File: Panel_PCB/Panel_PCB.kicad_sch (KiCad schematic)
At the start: 125 parts, among them J1 AC, J10 Relay 3, J11 Relay 4, J12 AC, J13 AC, J14 + de la bateria, J15 - de la bateria, J2 Bateria, J3 Sensor IN, J4 Sensor OUT, J5 Boton 1, J6 Boton 2, J7 Boton 3, J8 Relay 1, J9 Relay 2, K1 SANYOU_SRD_Form_C, K2 SANYOU_SRD_Form_C, K3 SANYOU_SRD_Form_C, K4 SANYOU_SRD_Form_C, K5 EC2-4.5SNU, K6 SANYOU_SRD_Form_C, K7 SANYOU_SRD_Form_C, Q1 2N2222A, Q2 2N2222A, Q3 2N2222A, Q4 2N2222A, Q5 BC558, Q6 BC558, Q7 2N2222A, U1 TLP291, U10 LM1117T-3.3, U11 LM7812_TO220, U2 TLP291, U3 TLP291, U4 TLP291, U5 LM7812_TO220, U6 LM7812_TO220, U7 LM7805_TO220, U8 LM7805_TO220, U9 LM1117T-3.3

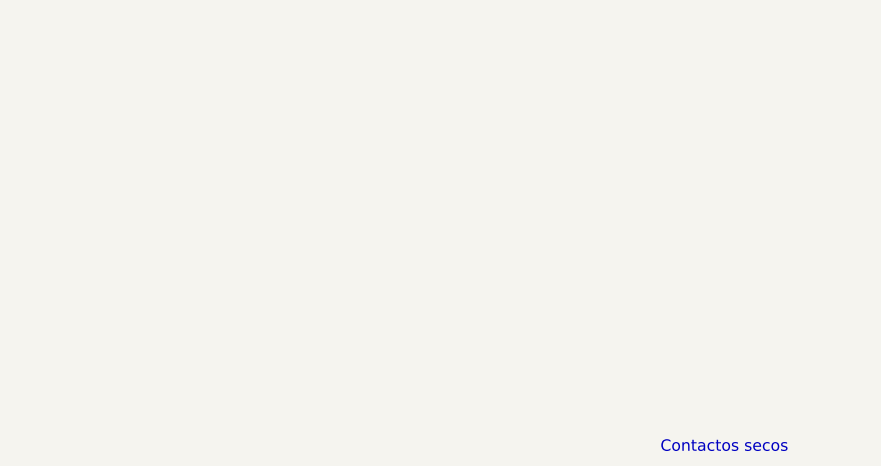
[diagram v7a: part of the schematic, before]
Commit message: DS1307 y bateria para mantener la hora actualizada
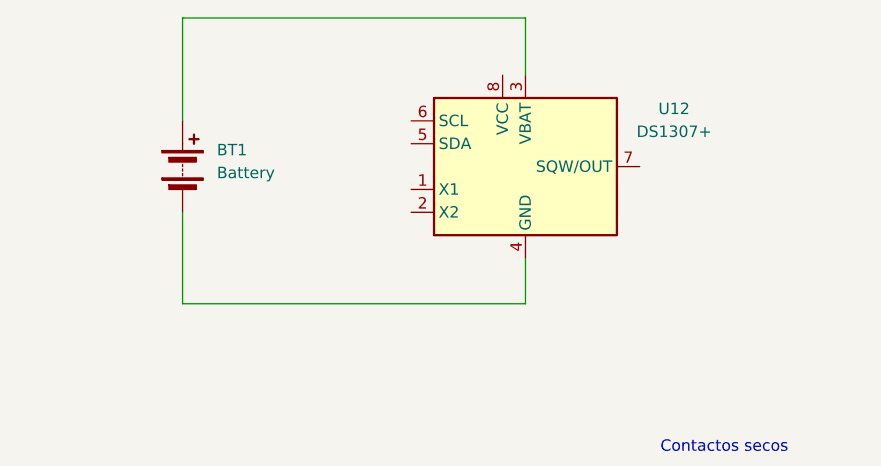
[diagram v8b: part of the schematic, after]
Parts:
- added BT1: Battery, Battery:BatteryHolder_Keystone_1060_1x2032, symbol Device:Battery
- added U12: DS1307+, Package_DIP:DIP-8_W7.62mm, symbol Timer_RTC:DS1307+
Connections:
- new net: BT1.1 (+), U12.3 (VBAT)
- new net: BT1.2 (-), U12.4 (GND)
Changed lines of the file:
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@@
 	(wire
 		(pts
+			(xy 445.77 72.39) (xy 445.77 67.31)
+		)
+		(stroke
+			(width 0)
+			(type default)
+			(color 0 0 0 1)
+		)
+	)
+	(wire
+		(pts
 			(xy 534.67 283.21) (xy 621.03 283.21)
 		)
@@
 	(wire
 		(pts
+			(xy 407.67 40.64) (xy 445.77 40.64)
+		)
+		(stroke
+			(width 0)
+			(type default)
+			(color 255 0 0 1)
+		)
+	)
+	(wire
+		(pts
 			(xy 154.94 110.49) (xy 154.94 120.65)
 		)
@@
 	(wire
 		(pts
+			(xy 445.77 40.64) (xy 445.77 46.99)
+		)
+		(stroke
+			(width 0)
+			(type default)
+			(color 255 0 0 1)
+		)
+	)
+	(wire
+		(pts
 			(xy 549.91 381) (xy 549.91 398.78)
 		)
@@
 	(wire
 		(pts
+			(xy 407.67 62.23) (xy 407.67 72.39)
+		)
+		(stroke
+			(width 0)
+			(type default)
+			(color 0 0 0 1)
+		)
+	)
+	(wire
+		(pts
 			(xy 273.05 233.68) (xy 273.05 247.65)
 		)
@@
 	(wire
 		(pts
+			(xy 407.67 52.07) (xy 407.67 40.64)
+		)
+		(stroke
+			(width 0)
+			(type default)
+			(color 255 0 0 1)
+		)
+	)
+	(wire
+		(pts
 			(xy 403.86 466.09) (xy 415.29 466.09)
 		)
@@
 	(wire
 		(pts
+			(xy 407.67 72.39) (xy 445.77 72.39)
+		)
+		(stroke
+			(width 0)
+			(type default)
+			(color 0 0 0 1)
+		)
+	)
+	(wire
+		(pts
 			(xy 403.86 300.99) (xy 403.86 339.09)
 		)
@@
 	)
 	(symbol
+		(lib_id "Device:Battery")
+		(at 407.67 57.15 0)
+		(unit 1)
+		(exclude_from_sim no)
+		(in_bom yes)
+		(on_board yes)
+		(dnp no)
+		(fields_autoplaced yes)
+		(property "Reference" "BT1"
+			(at 411.48 55.3084 0)
+			(effects
+				(font
+					(size 1.27 1.27)
+				)
+				(justify left)
+			)
+		)
+		(property "Value" "Battery"
+			(at 411.48 57.8484 0)
+			(effects
+				(font
+					(size 1.27 1.27)
+				)
+				(justify left)
+			)
+		)
+		(property "Footprint" "Battery:BatteryHolder_Keystone_1060_1x2032"
+			(at 407.67 55.626 90)
+			(effects
+				(font
+					(size 1.27 1.27)
+				)
+				(hide yes)
+			)
+		)
+		(property "Datasheet" "~"
+			(at 407.67 55.626 90)
+			(effects
+				(font
+					(size 1.27 1.27)
+				)
+				(hide yes)
+			)
+		)
+		(property "Description" "Multiple-cell battery"
+			(at 407.67 57.15 0)
+			(effects
+				(font
+					(size 1.27 1.27)
+				)
+				(hide yes)
+			)
+		)
+		(property "Sim.Device" "V"
+			(at 407.67 57.15 0)
+			(effects
+				(font
+					(size 1.27 1.27)
+				)
+				(hide yes)
+			)
+		)
+		(property "Sim.Type" "DC"
+			(at 407.67 57.15 0)
+			(effects
+				(font
+					(size 1.27 1.27)
+				)
+				(hide yes)
+			)
+		)
+		(property "Sim.Pins" "1=+ 2=-"
+			(at 407.67 57.15 0)
+			(effects
+				(font
+					(size 1.27 1.27)
+				)
+				(hide yes)
+			)
+		)
+		(pin "1"
+		)
+		(pin "2"
+		)
+		(instances
+			(project ""
+				(path "/f7146f60-4eeb-4a38-9050-767b0cc7f13c"
+					(reference "BT1")
+					(unit 1)
+				)
+			)
+		)
+	)
+	(symbol
 		(lib_id "Device:C_US")
 		(at 342.9 257.81 0)
@@
 					(unit 1)
 				)
+			)
+		)
+	)
+	(symbol
+		(lib_id "Timer_RTC:DS1307+")
+		(at 445.77 57.15 0)
+		(unit 1)
+		(exclude_from_sim no)
+		(in_bom yes)
+		(on_board yes)
+		(dnp no)
+		(fields_autoplaced yes)
+		(property "Reference" "U12"
+			(at 462.28 50.7298 0)
+			(effects
+				(font
+					(size 1.27 1.27)
+				)
+			)
+		)
+		(property "Value" "DS1307+"
+			(at 462.28 53.2698 0)
+			(effects
+				(font
+					(size 1.27 1.27)
+				)
+			)
+		)
+		(property "Footprint" "Package_DIP:DIP-8_W7.62mm"
+			(at 445.77 69.85 0)
+			(effects
+				(font
+					(size 1.27 1.27)
+				)
+				(hide yes)
+			)
+		)
+		(property "Datasheet" "https://datasheets.maximintegrated.com/en/ds/DS1307.pdf"
+			(at 445.77 62.23 0)
+			(effects
+				(font
+					(size 1.27 1.27)
+				)
+				(hide yes)
+			)
+		)
+		(property "Description" "64 x 8, Serial, I2C Real-time clock, 4.5V to 5.5V VCC, 0°C to +70°C, DIP-8"
+			(at 445.77 57.15 0)
+			(effects
+				(font
+					(size 1.27 1.27)
+				)
+				(hide yes)
+			)
+		)
+		(pin "1"
+		)
+		(pin "8"
+		)
+		(pin "4"
+		)
+		(pin "7"
+		)
+		(pin "3"
+		)
+		(pin "2"
+		)
+		(pin "6"
+		)
+		(pin "5"
+		)
+		(instances
+			(project ""
+				(path "/f7146f60-4eeb-4a38-9050-767b0cc7f13c"
+					(reference "U12")
+					(unit 1)
+				)
